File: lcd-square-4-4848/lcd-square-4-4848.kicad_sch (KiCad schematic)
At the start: 37 parts, among them J1 SWD, J2 Conn_01x40_MountingPin, SW1 BOOT0, SW2 RST, U1 siplex-som-s16, U2 TPS61169

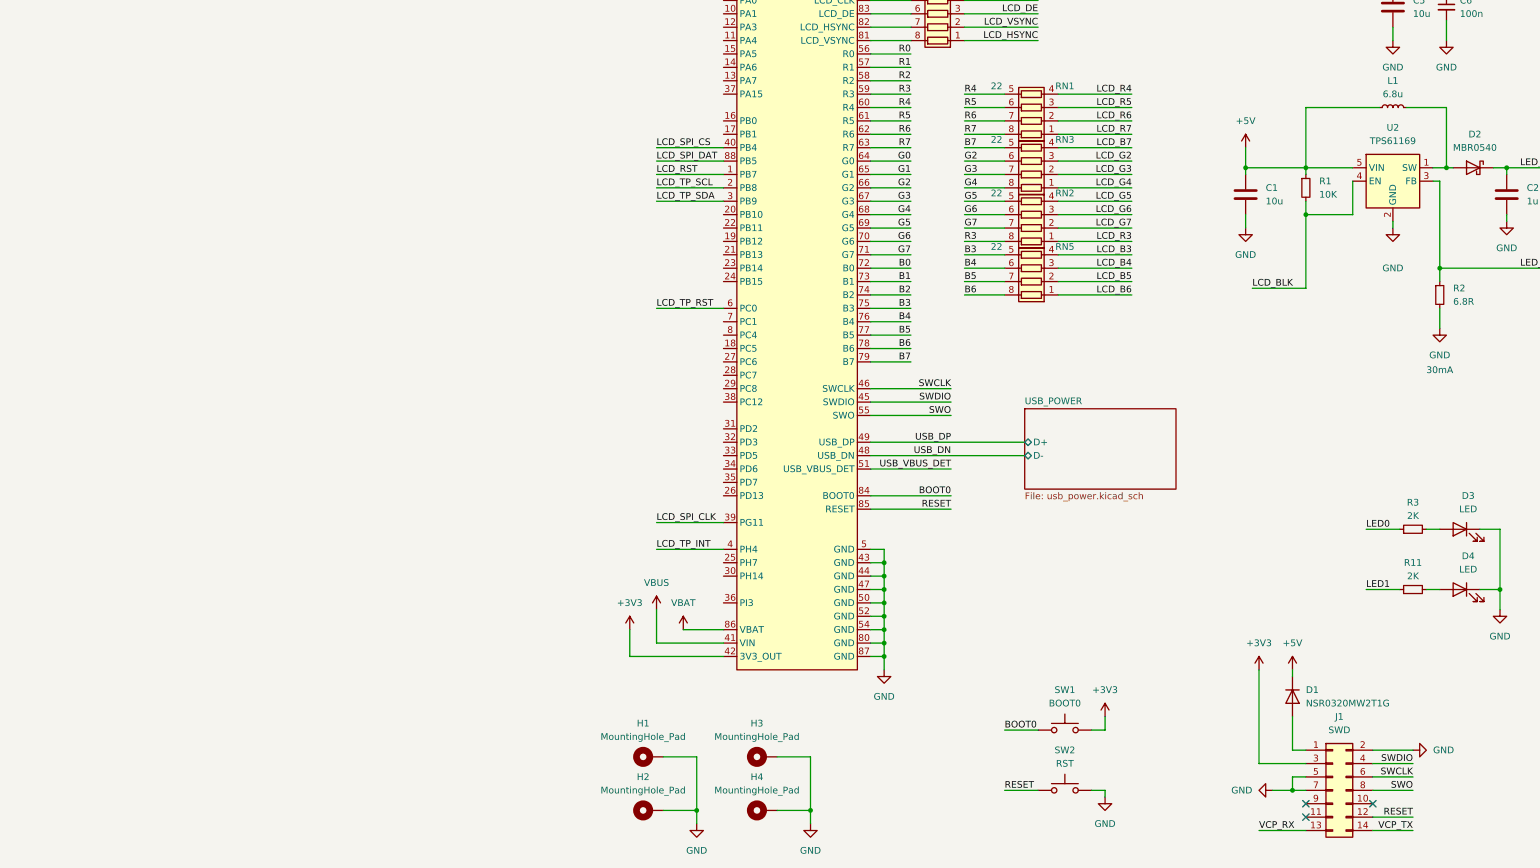
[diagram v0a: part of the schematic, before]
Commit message: LCD 4inch 480-480 on progress
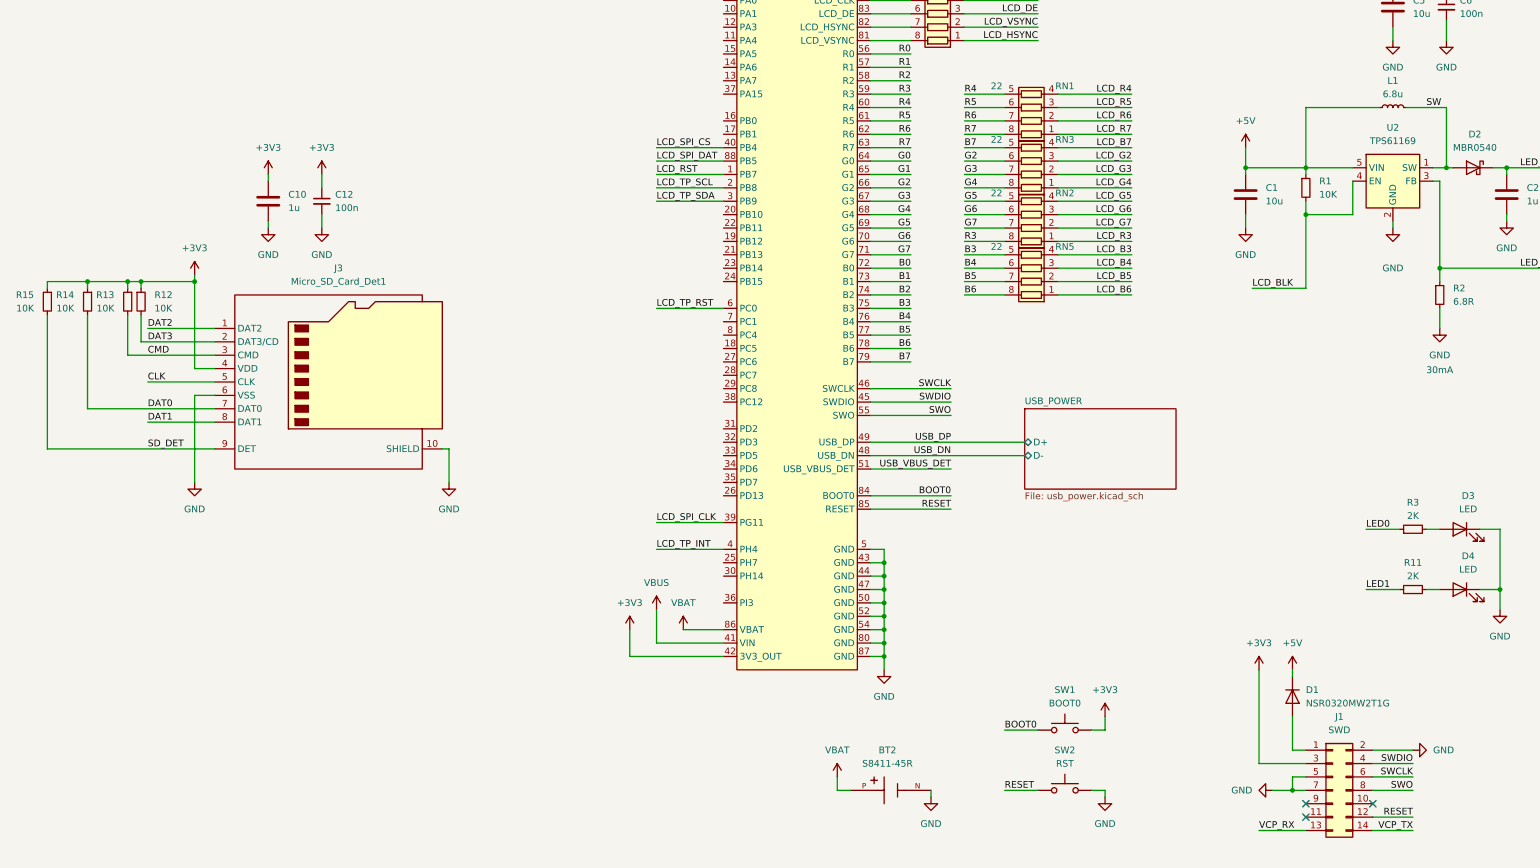
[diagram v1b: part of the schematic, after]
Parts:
- removed H1, H2, H3, H4: MountingHole_Pad, MountingHole:MountingHole_3.5mm_Pad_TopOnly, symbol Mechanical:MountingHole_Pad
- added BT2: S8411-45R, CR1220-Batt-conn-S8411-45R:CR1220-Batt-conn-S8411-45R, symbol CR1220-Batt-conn-S8411-45R:S8411-45R
- added C10: 1u, Capacitor_SMD:C_0603_1608Metric, symbol Device:C
- added C12: 100n, Capacitor_SMD:C_0402_1005Metric, symbol Device:C_Small
- added J3: Micro_SD_Card_Det1, TF-115:SD-TF-115, symbol Connector:Micro_SD_Card_Det1
- added R12, R13, R14, R15: 10K, Resistor_SMD:R_0402_1005Metric, symbol Device:R_Small
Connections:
- net +3V3: now also C10.1, C12.1, J3.4 (VDD), R12.1, R13.1, R14.1, R15.1
- net GND: now also BT2.N, C10.2, C12.2, J3.10 (SHIELD), J3.6 (VSS)
- net VBAT: now also BT2.P
- net SW: now reaches D2.2 (A), L1.2, U2.1 (SW)
- new net CLK: J3.5 (CLK)
- new net CMD: J3.3 (CMD), R13.2
- new net DAT0: J3.7 (DAT0), R14.2
- new net DAT1: J3.8 (DAT1)
- new net DAT2: J3.1 (DAT2)
- new net DAT3: J3.2 (DAT3/CD), R12.2
- new net SD_DET: J3.9 (DET), R15.2

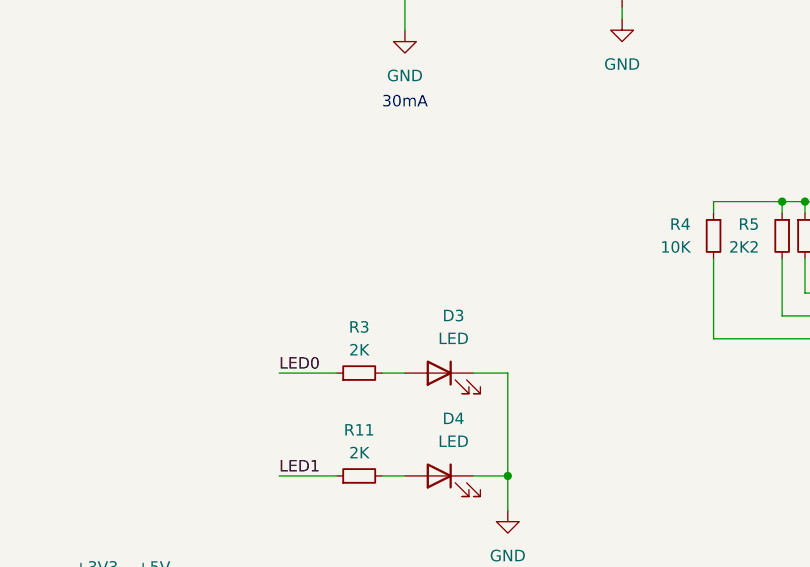
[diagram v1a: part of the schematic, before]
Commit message: Change SD card orientation
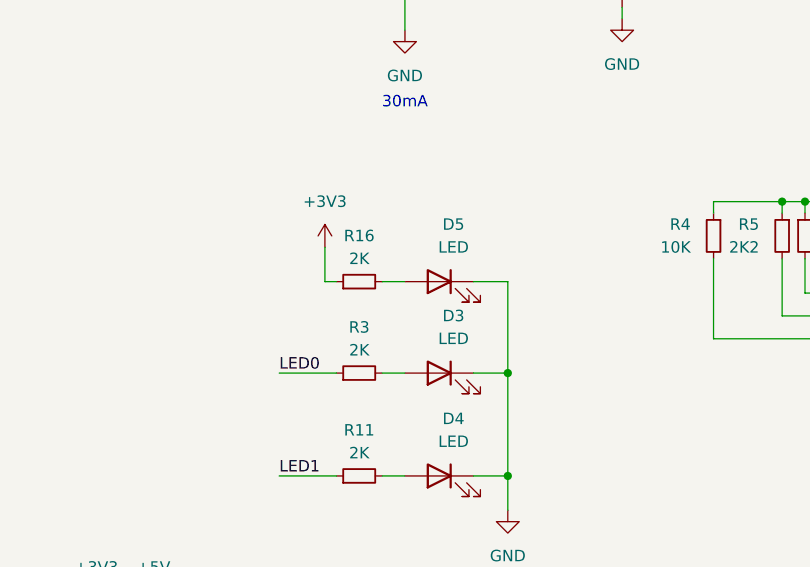
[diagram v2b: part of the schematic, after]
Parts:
- added D5: LED, LED_SMD:LED_0805_2012Metric, symbol Device:LED
- added R16: 2K, Resistor_SMD:R_0402_1005Metric, symbol Device:R_Small
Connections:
- net +3V3: now also R16.1
- net GND: now also D5.1 (K)
- new net: D5.2 (A), R16.2

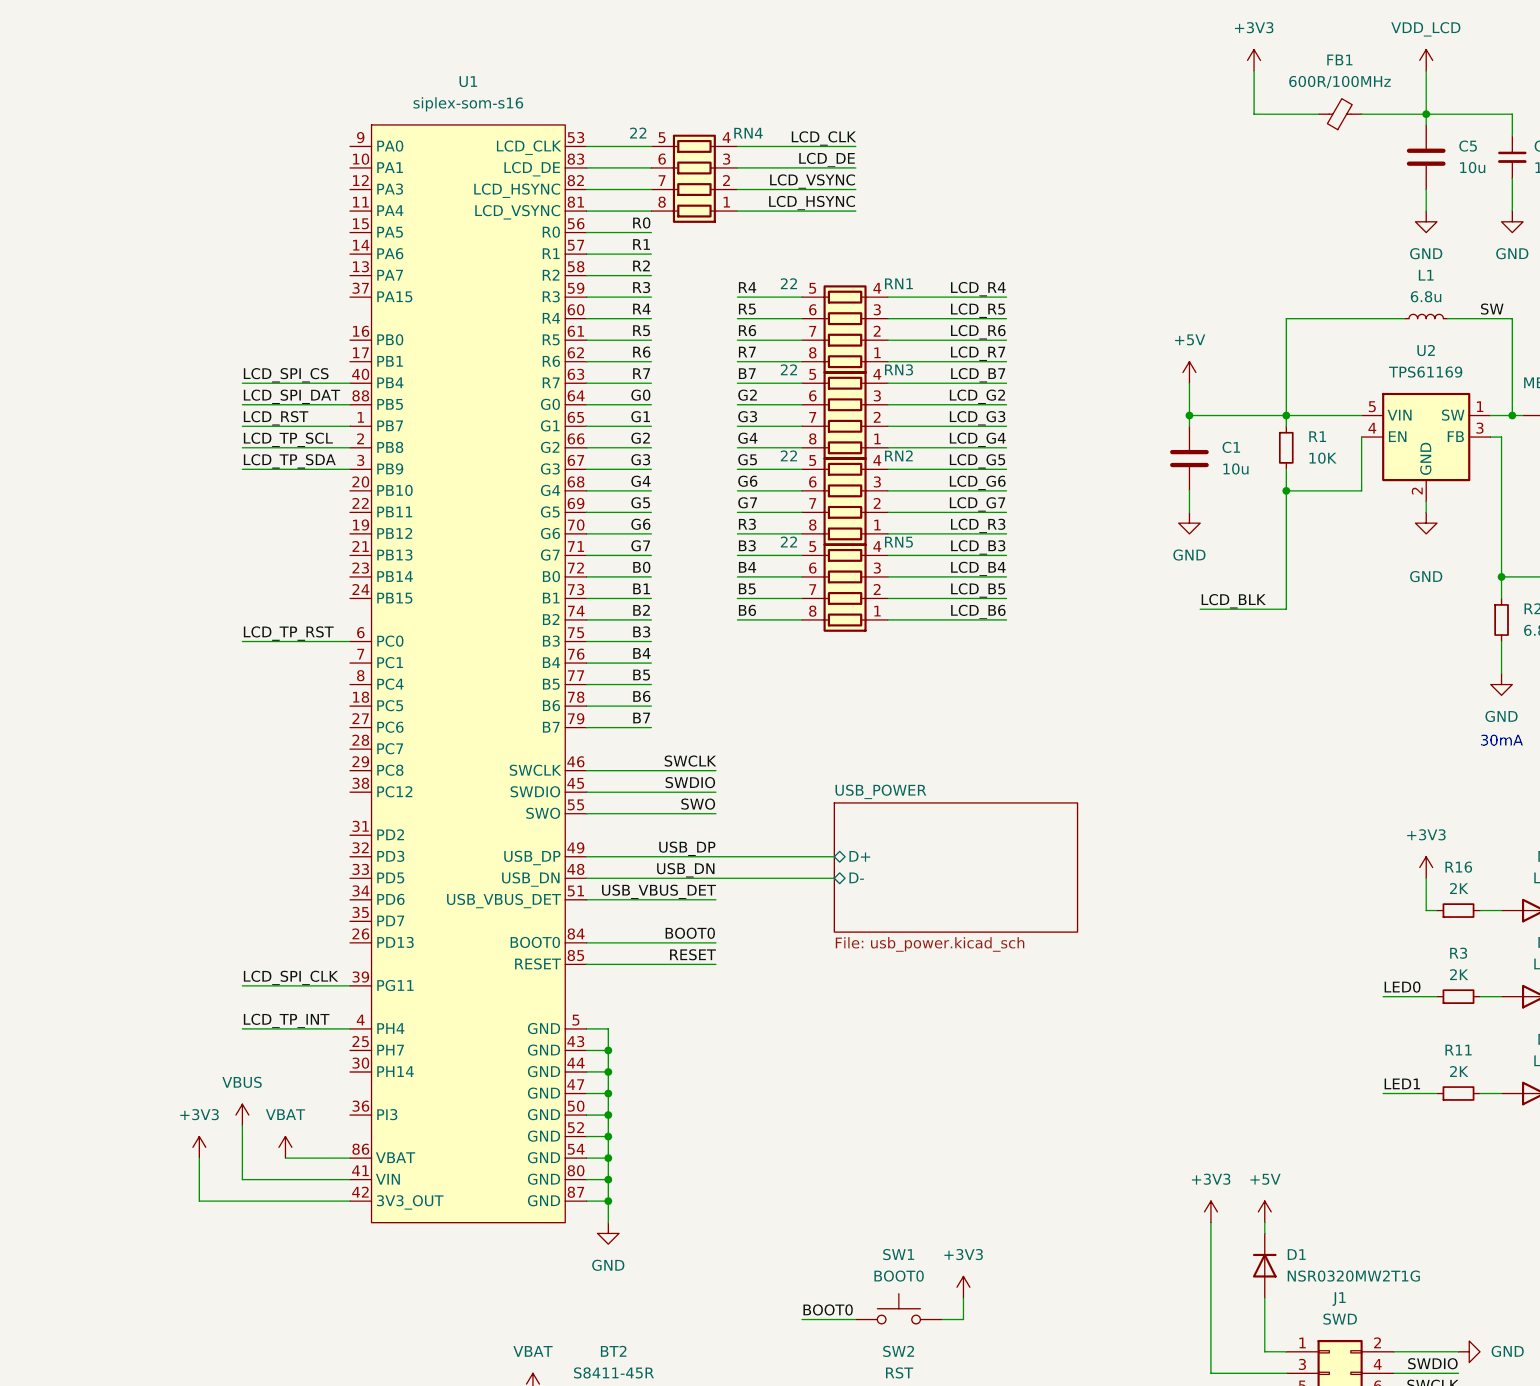
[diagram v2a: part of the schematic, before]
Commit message: LCD 4inch 480x480 98% finished, st-link left
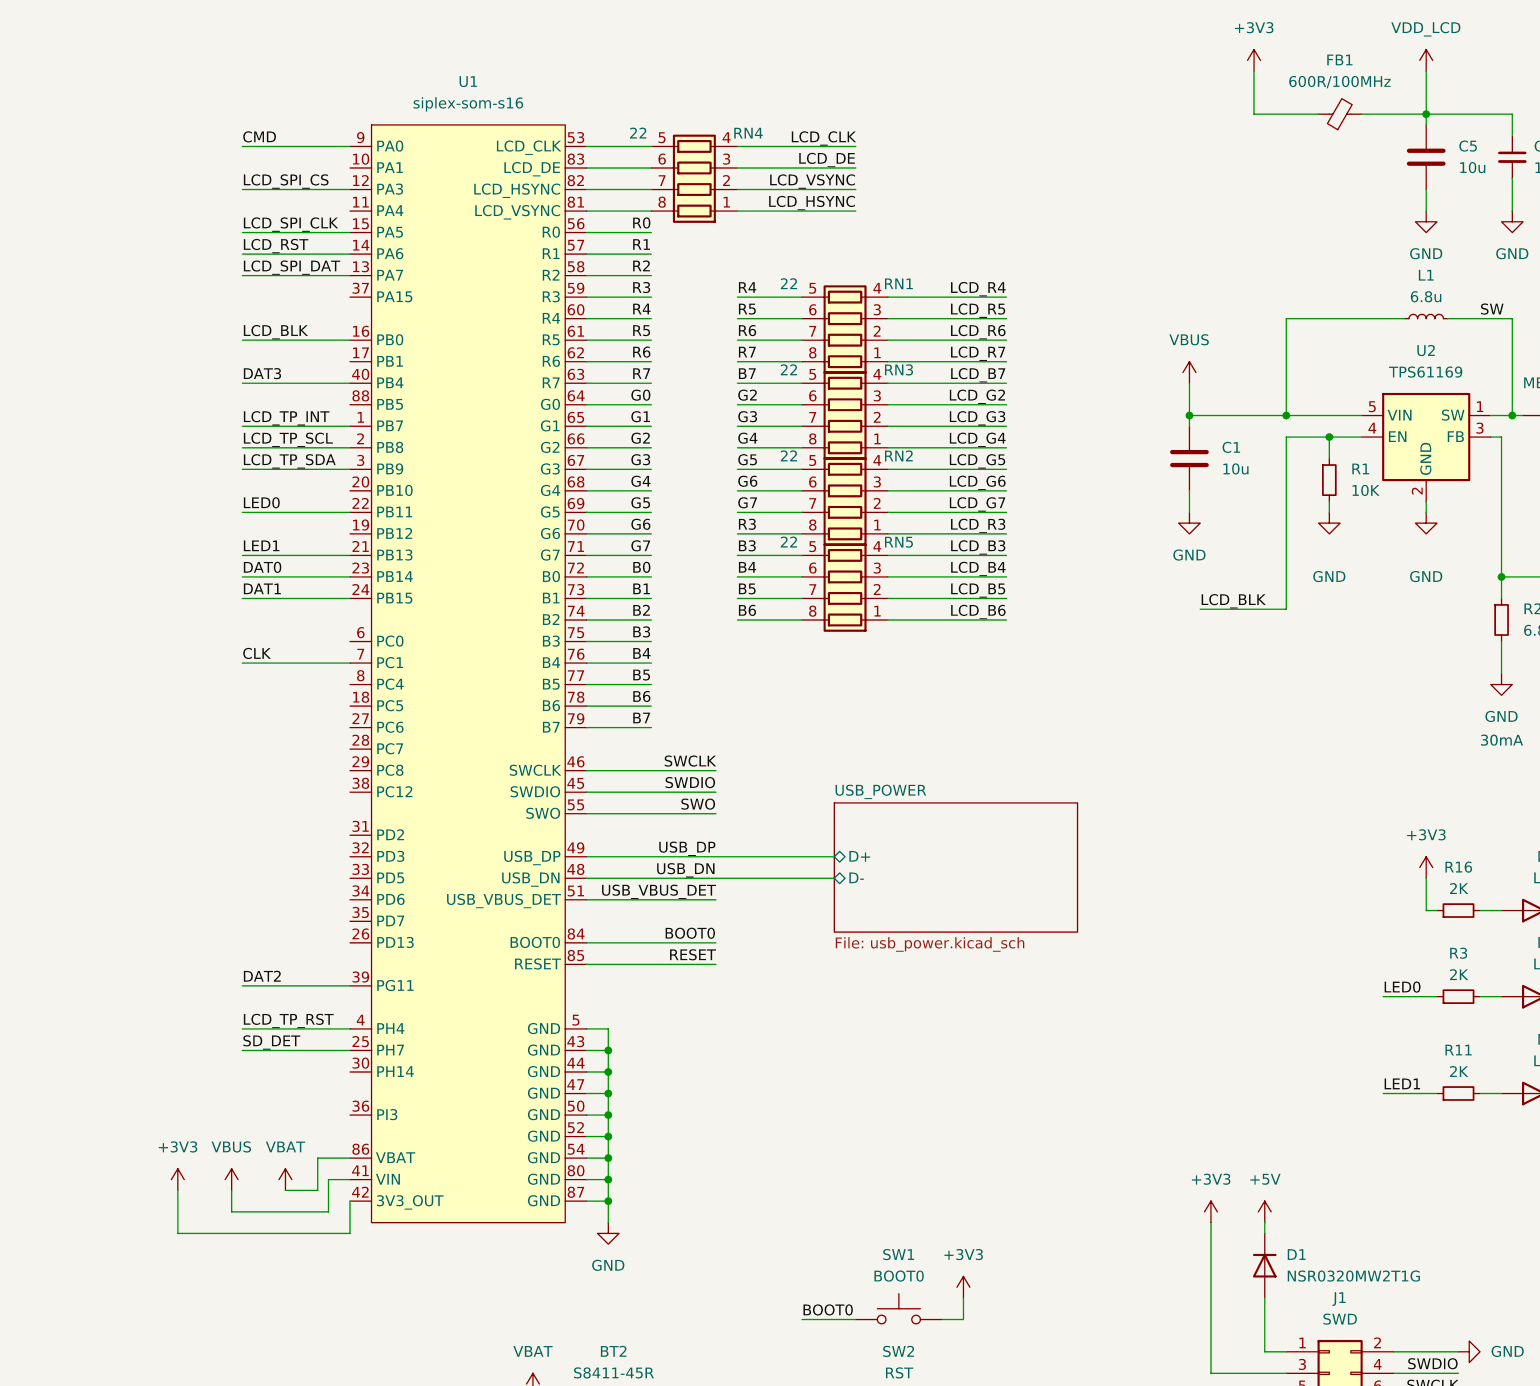
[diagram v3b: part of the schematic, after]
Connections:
- net +5V: no longer C1.1, L1.1, R1.1, U2.5 (VIN)
- net CLK: now also U1.7 (PC1)
- net CMD: now also U1.9 (PA0)
- net DAT0: now also U1.23 (PB14)
- net DAT1: now also U1.24 (PB15)
- net DAT2: now also U1.39 (PG11)
- net DAT3: now also U1.40 (PB4)
- net GND: now also R1.2
- net LCD_BLK: now also R1.1, U1.16 (PB0); no longer R1.2
- net LCD_RST: now also U1.14 (PA6); no longer U1.1 (PB7)
- net LCD_SPI_CLK: now also U1.15 (PA5); no longer U1.39 (PG11)
- net LCD_SPI_CS: now also U1.12 (PA3); no longer U1.40 (PB4)
- net LCD_SPI_DAT: now also U1.13 (PA7); no longer U1.88 (PB5)
- net LCD_TP_INT: now also U1.1 (PB7); no longer U1.4 (PH4)
- net LCD_TP_RST: now also U1.4 (PH4); no longer U1.6 (PC0)
- net LED0: now also U1.22 (PB11)
- net LED1: now also U1.21 (PB13)
- net SD_DET: now also U1.25 (PH7)
- net VBUS: now also C1.1, L1.1, U2.5 (VIN)
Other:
- moved on the sheet: R1
